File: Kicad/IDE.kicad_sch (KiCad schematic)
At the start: 16 parts, among them J3 LED, J4 Conn_02x22_Odd_Even, U3 74HCT245, U4 74HCT245, U5 74HCT245

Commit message: PCB: Fixups
* Tweak KEL connector hole sizes
* Fixup MT48LC8M16A2P - Had copied this from the 16M16 part and forgot to make A12 an NC
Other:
- company: (none) -> Matt Harlum
- title: (none) -> CIDER
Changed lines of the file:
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@@
 (kicad_sch (version 20211123) (generator eeschema)
   (paper "A4")
+  (title_block
+    (title "CIDER")
+    (company "Matt Harlum")
+  )
   (junction (at 92.71 139.065) (diameter 0) (color 0 0 0 0)
   )

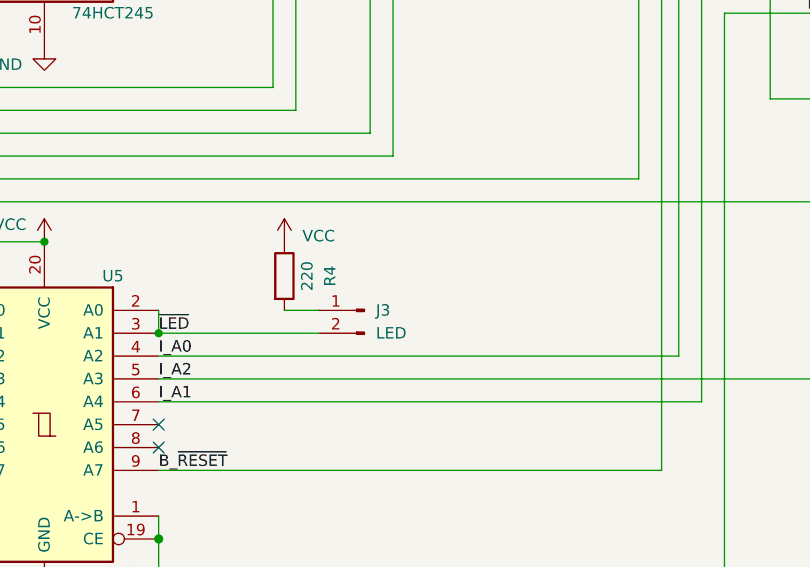
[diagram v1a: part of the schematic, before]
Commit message: Proto_B: Add A500 mode jumper, add SMD Act LED
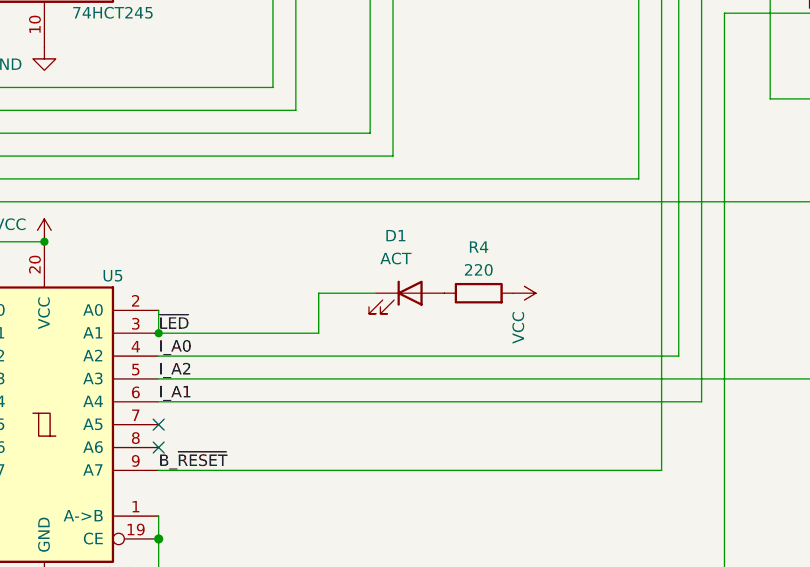
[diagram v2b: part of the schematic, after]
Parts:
- removed J3: LED, Connector_PinHeader_2.00mm:PinHeader_1x02_P2.00mm_Vertical, symbol Connector:Conn_01x02_Male
- added D1: ACT, LED_SMD:LED_0603_1608Metric, symbol Device:LED
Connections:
- net VCC: now also R4.2; no longer R4.1
- net ~{LED}: now also D1.1 (K)
- new net: D1.2 (A), R4.1
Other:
- moved on the sheet: R4
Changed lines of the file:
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@@
+    (stroke (width 0) (type default) (color 0 0 0 0))
+  )
+  (wire (pts (xy 123.19 144.78) (xy 129.54 144.78))
     (stroke (width 0) (type default) (color 0 0 0 0))
   )
@@
     (stroke (width 0) (type default) (color 0 0 0 0))
   )
-  (wire (pts (xy 119.38 146.685) (xy 123.19 146.685))
-    (stroke (width 0) (type solid) (color 0 0 0 0))
-  )
   (bus (pts (xy 114.935 40.005) (xy 114.935 42.545))
     (stroke (width 0) (type default) (color 0 0 0 0))
@@
   )
   (wire (pts (xy 142.24 53.34) (xy 142.24 50.8))
+    (stroke (width 0) (type default) (color 0 0 0 0))
+  )
+  (wire (pts (xy 123.19 149.225) (xy 123.19 144.78))
     (stroke (width 0) (type default) (color 0 0 0 0))
   )
@@
     (pin "1")
   )
-  (symbol (lib_id "Device:R") (at 119.38 142.875 0) (unit 1)
-    (in_bom yes) (on_board yes)
-    (property "Reference" "R4" (id 0) (at 124.46 142.875 90))
-    (property "Value" "220" (id 1) (at 121.92 142.875 90))
-    (property "Footprint" "Resistor_SMD:R_0603_1608Metric" (id 2) (at 117.602 142.875 90)
-      (effects (font (size 1.27 1.27)) hide)
-    )
-    (property "Datasheet" "~" (id 3) (at 119.38 142.875 0)
-      (effects (font (size 1.27 1.27)) hide)
-    )
-    (property "LCSC #" "C22962" (id 4) (at 119.38 142.875 90)
+  (symbol (lib_id "Device:R") (at 140.97 144.78 90) (unit 1)
+    (in_bom yes) (on_board yes)
+    (property "Reference" "R4" (id 0) (at 140.97 139.7 90))
+    (property "Value" "220" (id 1) (at 140.97 142.24 90))
+    (property "Footprint" "Resistor_SMD:R_0603_1608Metric" (id 2) (at 140.97 146.558 90)
+      (effects (font (size 1.27 1.27)) hide)
+    )
+    (property "Datasheet" "~" (id 3) (at 140.97 144.78 0)
+      (effects (font (size 1.27 1.27)) hide)
+    )
+    (property "LCSC #" "C22962" (id 4) (at 140.97 144.78 90)
       (effects (font (size 1.27 1.27)) hide)
     )
@@
     (pin "1")
   )
-  (symbol (lib_id "power:VCC") (at 119.38 139.065 0) (unit 1)
-    (in_bom yes) (on_board yes)
-    (property "Reference" "#PWR035" (id 0) (at 119.38 142.875 0)
-      (effects (font (size 1.27 1.27)) hide)
-    )
-    (property "Value" "VCC" (id 1) (at 123.19 138.43 0))
-    (property "Footprint" "" (id 2) (at 119.38 139.065 0)
-      (effects (font (size 1.27 1.27)) hide)
-    )
-    (property "Datasheet" "" (id 3) (at 119.38 139.065 0)
+  (symbol (lib_id "power:VCC") (at 144.78 144.78 270) (unit 1)
+    (in_bom yes) (on_board yes)
+    (property "Reference" "#PWR035" (id 0) (at 140.97 144.78 0)
+      (effects (font (size 1.27 1.27)) hide)
+    )
+    (property "Value" "VCC" (id 1) (at 145.415 148.59 0))
+    (property "Footprint" "" (id 2) (at 144.78 144.78 0)
+      (effects (font (size 1.27 1.27)) hide)
+    )
+    (property "Datasheet" "" (id 3) (at 144.78 144.78 0)
       (effects (font (size 1.27 1.27)) hide)
     )
@@
     )
     (pin "1")
-  )
-  (symbol (lib_id "Connector:Conn_01x02_Male") (at 128.27 146.685 0) (mirror y) (unit 1)
-    (in_bom yes) (on_board yes) (fields_autoplaced)
-    (property "Reference" "J3" (id 0) (at 129.54 146.6849 0)
-      (effects (font (size 1.27 1.27)) (justify right))
-    )
-    (property "Value" "LED" (id 1) (at 129.54 149.2249 0)
-      (effects (font (size 1.27 1.27)) (justify right))
-    )
-    (property "Footprint" "Connector_PinHeader_2.00mm:PinHeader_1x02_P2.00mm_Vertical" (id 2) (at 128.27 146.685 0)
-      (effects (font (size 1.27 1.27)) hide)
-    )
-    (property "Datasheet" "~" (id 3) (at 128.27 146.685 0)
-      (effects (font (size 1.27 1.27)) hide)
-    )
-    (pin "1")
-    (pin "2")
   )
   (symbol (lib_id "74xx:74HC245") (at 92.71 42.545 0) (mirror y) (unit 1)
@@
     (pin "1")
   )
+  (symbol (lib_id "Device:LED") (at 133.35 144.78 0) (unit 1)
+    (in_bom yes) (on_board yes) (fields_autoplaced)
+    (property "Reference" "D1" (id 0) (at 131.7625 138.43 0))
+    (property "Value" "ACT" (id 1) (at 131.7625 140.97 0))
+    (property "Footprint" "LED_SMD:LED_0603_1608Metric" (id 2) (at 133.35 144.78 0)
+      (effects (font (size 1.27 1.27)) hide)
+    )
+    (property "Datasheet" "~" (id 3) (at 133.35 144.78 0)
+      (effects (font (size 1.27 1.27)) hide)
+    )
+    (property "LCSC #" "C264450" (id 4) (at 133.35 144.78 0)
+      (effects (font (size 1.27 1.27)) hide)
+    )
+    (pin "1")
+    (pin "2")
+  )
   (symbol (lib_id "power:VCC") (at 25.4 182.88 0) (unit 1)

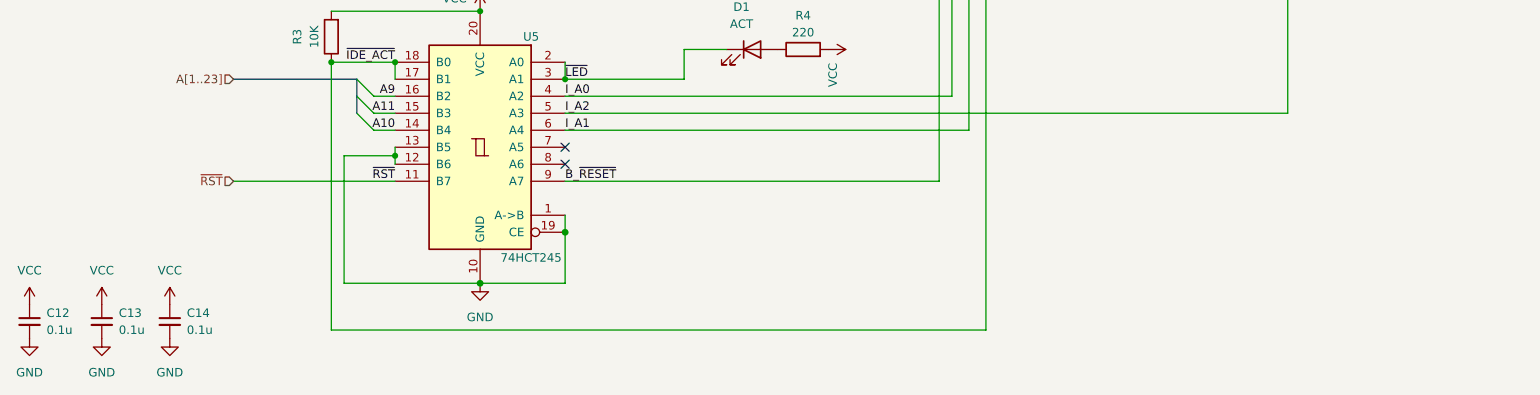
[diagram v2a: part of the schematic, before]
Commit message: Rev-A1: Buffer A500/Bank Sel switches
Added inline resistors to these two and buffer them via U5
In Proto A it was found that operating the switches would cause latch-up and destroy the CPLD
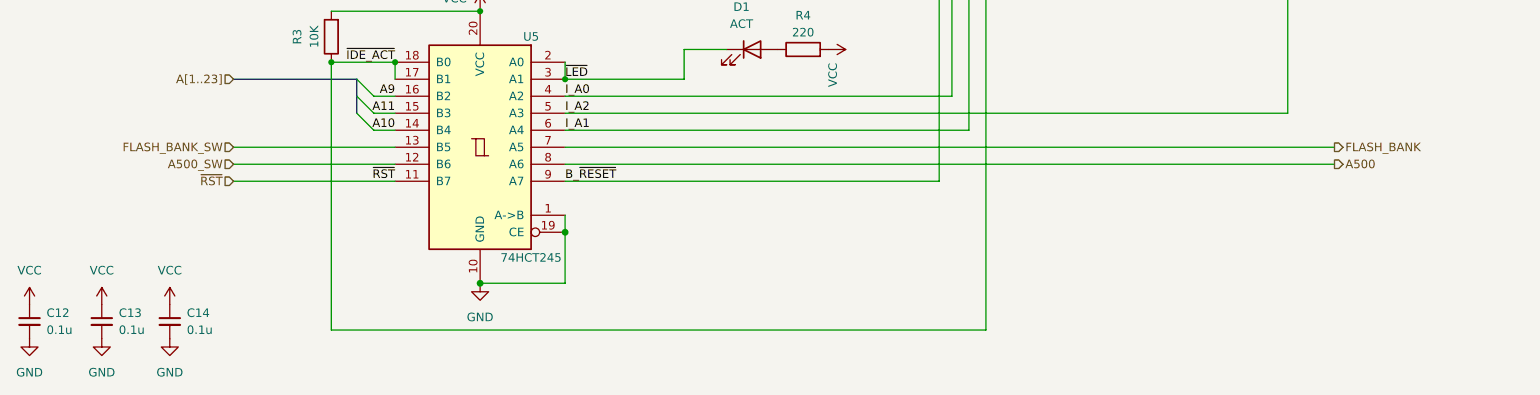
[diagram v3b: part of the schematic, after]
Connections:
- net GND: no longer U5.12 (B6), U5.13 (B5)
- net FLASH_BANK: now reaches U5.7 (A5)
- net A500: now reaches U5.8 (A6)
- new net A500_SW: U5.12 (B6)
- new net FLASH_BANK_SW: U5.13 (B5)
- no-connect marks 6 -> 4
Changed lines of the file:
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@@
   (junction (at 92.71 139.065) (diameter 0) (color 0 0 0 0)
   )
-  (junction (at 80.01 160.655) (diameter 0) (color 0 0 0 0)
-  )
   (junction (at 120.65 109.855) (diameter 0) (color 0 0 0 0)
   )
@@
   )
   (no_connect (at 184.785 90.805))
-  (no_connect (at 105.41 159.385))
-  (no_connect (at 105.41 161.925))
   (no_connect (at 197.485 103.505))
   (no_connect (at 197.485 106.045))
@@
     (stroke (width 0) (type default) (color 0 0 0 0))
   )
+  (wire (pts (xy 105.41 161.925) (xy 220.345 161.925))
+    (stroke (width 0) (type default) (color 0 0 0 0))
+  )
   (bus (pts (xy 74.295 151.765) (xy 74.295 149.225))
     (stroke (width 0) (type default) (color 0 0 0 0))
@@
     (stroke (width 0) (type default) (color 0 0 0 0))
   )
+  (wire (pts (xy 105.41 159.385) (xy 220.345 159.385))
+    (stroke (width 0) (type default) (color 0 0 0 0))
+  )
   (wire (pts (xy 172.085 70.485) (xy 175.895 70.485))
     (stroke (width 0) (type default) (color 0 0 0 0))
@@
     (stroke (width 0) (type default) (color 0 0 0 0))
   )
-  (wire (pts (xy 72.39 160.655) (xy 80.01 160.655))
-    (stroke (width 0) (type default) (color 0 0 0 0))
-  )
   (wire (pts (xy 197.485 70.485) (xy 209.55 70.485))
     (stroke (width 0) (type default) (color 0 0 0 0))
@@
     (stroke (width 0) (type default) (color 0 0 0 0))
   )
-  (wire (pts (xy 80.01 159.385) (xy 80.01 160.655))
-    (stroke (width 0) (type solid) (color 0 0 0 0))
-  )
   (bus (pts (xy 73.025 97.155) (xy 73.025 94.615))
     (stroke (width 0) (type default) (color 0 0 0 0))
@@
     (stroke (width 0) (type default) (color 0 0 0 0))
   )
+  (wire (pts (xy 55.88 161.925) (xy 80.01 161.925))
+    (stroke (width 0) (type default) (color 0 0 0 0))
+  )
   (wire (pts (xy 213.36 154.305) (xy 213.36 108.585))
     (stroke (width 0) (type default) (color 0 0 0 0))
@@
     (stroke (width 0) (type default) (color 0 0 0 0))
   )
-  (wire (pts (xy 80.01 160.655) (xy 80.01 161.925))
-    (stroke (width 0) (type solid) (color 0 0 0 0))
-  )
   (wire (pts (xy 80.01 146.685) (xy 80.01 149.225))
     (stroke (width 0) (type default) (color 0 0 0 0))
@@
     (stroke (width 0) (type default) (color 0 0 0 0))
   )
-  (wire (pts (xy 72.39 179.705) (xy 92.71 179.705))
-    (stroke (width 0) (type default) (color 0 0 0 0))
-  )
   (bus (pts (xy 114.935 34.925) (xy 114.935 37.465))
     (stroke (width 0) (type default) (color 0 0 0 0))
@@
     (stroke (width 0) (type solid) (color 0 0 0 0))
   )
-  (wire (pts (xy 72.39 160.655) (xy 72.39 179.705))
+  (wire (pts (xy 55.88 159.385) (xy 80.01 159.385))
     (stroke (width 0) (type default) (color 0 0 0 0))
   )
@@
     (effects (font (size 1.27 1.27)) (justify right))
   )
+  (hierarchical_label "A500" (shape output) (at 220.345 161.925 0)
+    (effects (font (size 1.27 1.27)) (justify left))
+  )
   (hierarchical_label "~{IORD}" (shape input) (at 55.88 129.54 180)
     (effects (font (size 1.27 1.27)) (justify right))
@@
     (effects (font (size 1.27 1.27)) (justify right))
   )
+  (hierarchical_label "FLASH_BANK_SW" (shape input) (at 55.88 159.385 180)
+    (effects (font (size 1.27 1.27)) (justify right))
+  )
   (hierarchical_label "~{IOWR}" (shape input) (at 55.88 127 180)
     (effects (font (size 1.27 1.27)) (justify right))
@@
     (effects (font (size 1.27 1.27)) (justify right))
   )
+  (hierarchical_label "FLASH_BANK" (shape output) (at 220.345 159.385 0)
+    (effects (font (size 1.27 1.27)) (justify left))
+  )
   (hierarchical_label "~{RST}" (shape input) (at 55.88 164.465 180)
     (effects (font (size 1.27 1.27)) (justify right))
   )
+  (hierarchical_label "A500_SW" (shape input) (at 55.88 161.925 180)
+    (effects (font (size 1.27 1.27)) (justify right))
+  )
